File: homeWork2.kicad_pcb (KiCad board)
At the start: 2 copper layers, 36 parts, among them J4 0.100_2Pin, J5 0.100_2Pin, U1 LM7805_TO220

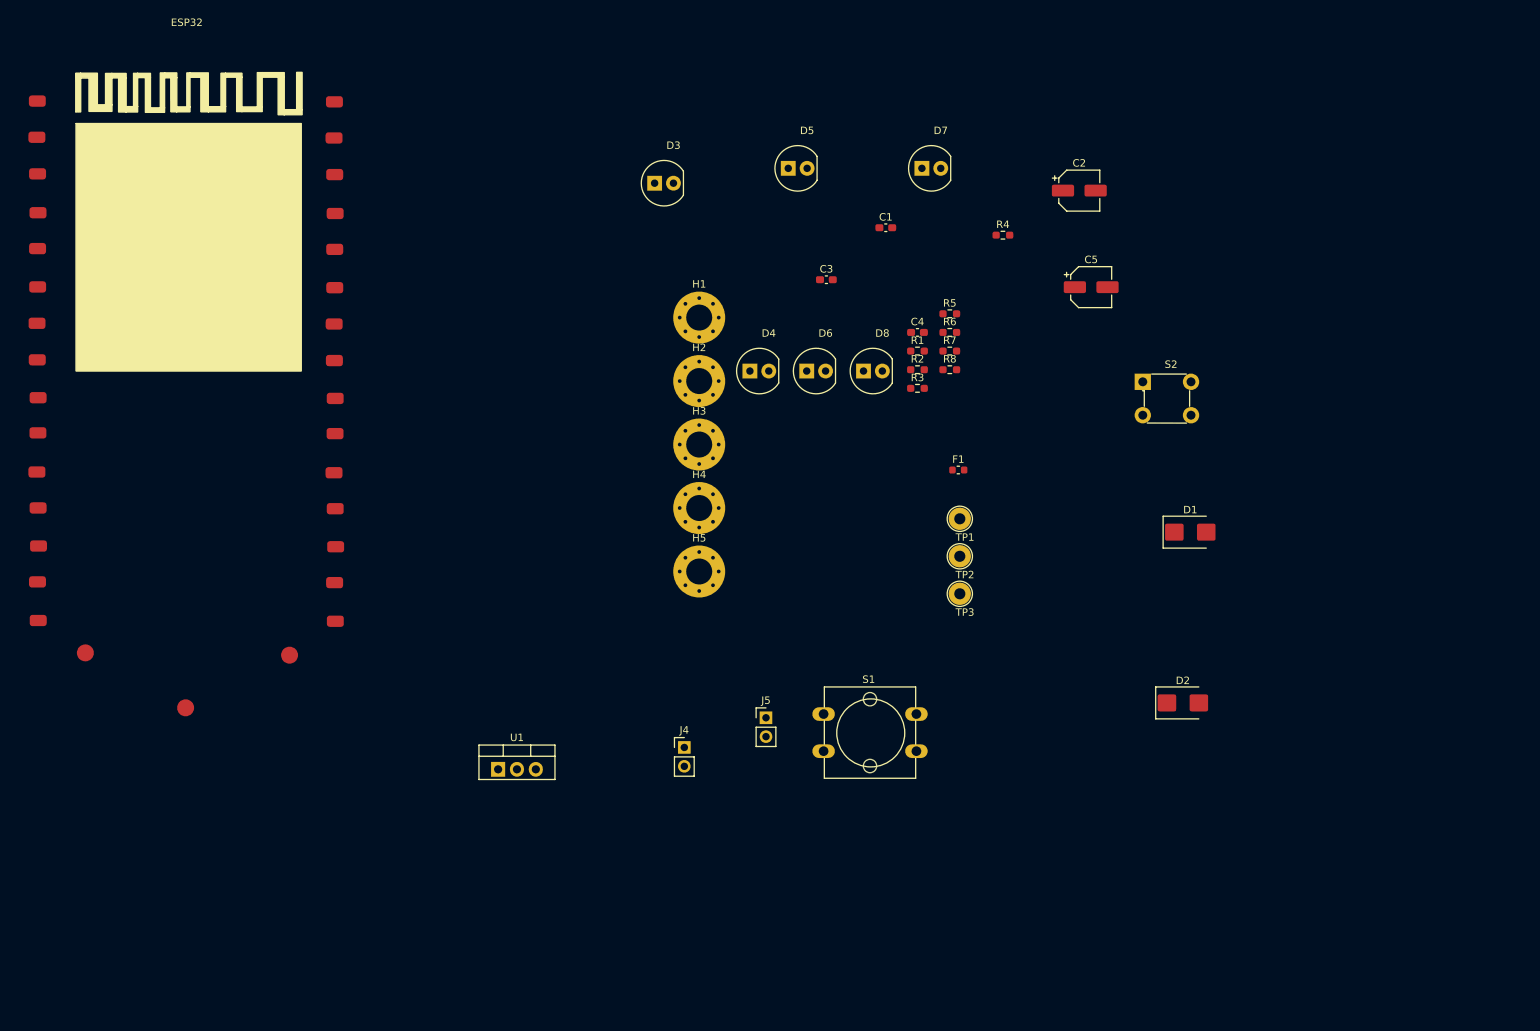
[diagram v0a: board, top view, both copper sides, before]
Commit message: Schematic changes
the ESP32 symbol library is not saved in the same folder of the project and linked to the footprint library
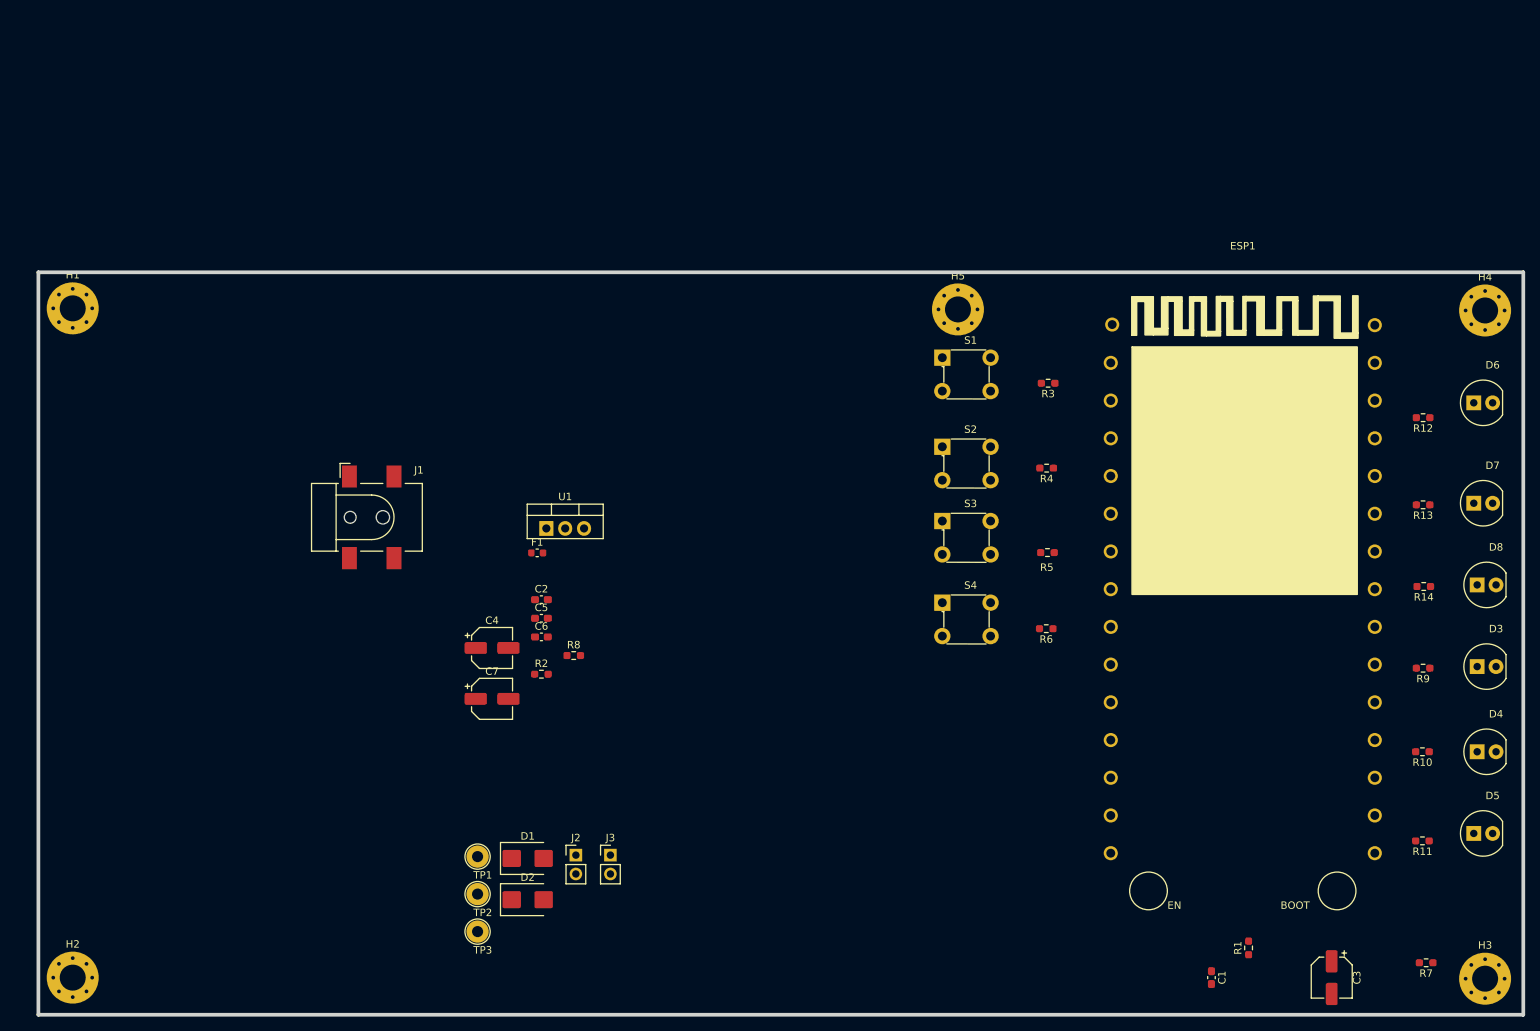
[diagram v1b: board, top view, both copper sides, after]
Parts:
- removed ESP32: ~, esp32 15 pin Library:esp32
- removed J4, J5: 0.100_2Pin, Connector_PinHeader_2.54mm:PinHeader_1x02_P2.54mm_Vertical
- added C6: 100nF, Capacitor_SMD:C_0603_1608Metric_Pad1.08x0.95mm_HandSolder, F.Cu at (117.8, 99.1)
- added C7: 47uF 16V, Capacitor_SMD:CP_Elec_5x5.4, F.Cu at (111.1, 107.5)
- added ESP1: ~, esp32 15 pin Library:esp32, F.Cu at (212.2, 47.0)
- added J1: Barrel_Jack_Switch_SMT, PubInv_KiCad_PCB:BarrelJack_CLIFF_FC681465S_SMT_Horizontal, F.Cu at (94.9, 83.0)
- added J2: 0.100_2Pin, Connector_PinHeader_2.54mm:PinHeader_1x02_P2.54mm_Vertical, F.Cu at (122.4, 128.5)
- added J3: 0.100_2Pin, Connector_PinHeader_2.54mm:PinHeader_1x02_P2.54mm_Vertical, F.Cu at (127.0, 128.5)
- added R10: 330R, Resistor_SMD:R_0603_1608Metric_Pad0.98x0.95mm_HandSolder, F.Cu at (236.4, 114.6)
- added R11: 330R, Resistor_SMD:R_0603_1608Metric_Pad0.98x0.95mm_HandSolder, F.Cu at (236.4, 126.6)
- added R12: 330R, Resistor_SMD:R_0603_1608Metric_Pad0.98x0.95mm_HandSolder, F.Cu at (236.5, 69.6)
- added R13: 330R, Resistor_SMD:R_0603_1608Metric_Pad0.98x0.95mm_HandSolder, F.Cu at (236.5, 81.3)
- added R14: 330R, Resistor_SMD:R_0603_1608Metric_Pad0.98x0.95mm_HandSolder, F.Cu at (236.6, 92.3)
- added R9: 330R, Resistor_SMD:R_0603_1608Metric_Pad0.98x0.95mm_HandSolder, F.Cu at (236.5, 103.3)
- added S3: SWITCH_TACTILE_SPST-NO_0.05A_24V, PubInv_KiCad_PCB:Switch_Tactile_THT_6x6mm, F.Cu at (171.8, 83.5)
- added S4: SWITCH_TACTILE_SPST-NO_0.05A_24V, PubInv_KiCad_PCB:Switch_Tactile_THT_6x6mm, F.Cu at (171.8, 94.5)
- C1: value 39pF -> 100nF
- C2: value 47uF 16V -> 39pF; footprint Capacitor_SMD:CP_Elec_5x5.4 -> Capacitor_SMD:C_0603_1608Metric_Pad1.08x0.95mm_HandSolder
- C3, C4: value 100nF -> 47uF 16V; footprint Capacitor_SMD:C_0603_1608Metric_Pad1.08x0.95mm_HandSolder -> Capacitor_SMD:CP_Elec_5x5.4
- C5: value 47uF 16V -> 100nF; footprint Capacitor_SMD:CP_Elec_5x5.4 -> Capacitor_SMD:C_0603_1608Metric_Pad1.08x0.95mm_HandSolder
- R1: value DNI -> 1R0
- R3, R4, R5, R6: value 330R -> 10K
- R7: value 330R -> 1R0
- R8: value 330R -> DNI
- S1: value SWITCH_TACTILE_12mmx12mm_SPST-NO_0.05A_24V -> SWITCH_TACTILE_SPST-NO_0.05A_24V; footprint PubInv_KiCad_PCB:SW_PUSH-12mm_WithCap_Green -> PubInv_KiCad_PCB:Switch_Tactile_THT_6x6mm
- moved D5 128.6 mm to (245.9, 125.6)
- moved D3 128.5 mm to (246.3, 103.1)
- moved H3 128.0 mm to (244.9, 145.1)
- moved H2 116.5 mm to (54.6, 145.0)
- moved C3 116.1 mm to (224.2, 145.0), turned to -90 degrees
- moved D4 110.6 mm to (246.3, 114.6)
- moved C1 110.1 mm to (208.0, 145.0), turned to -90 degrees
- moved H4 109.1 mm to (244.9, 55.1)
- moved R7 104.4 mm to (236.9, 143.0), turned to 180 degrees
- moved D1 99.5 mm to (115.9, 128.9)
- moved D2 92.1 mm to (115.9, 134.5)
- moved R1 91.9 mm to (213.0, 141.0), turned to 90 degrees
- moved C2 91.0 mm to (117.8, 94.1)
- moved D6 89.9 mm to (245.9, 67.6)
- moved D8 87.5 mm to (246.3, 92.1)
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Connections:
- C1 pad 1: GND -> Net-(ESP1-VIN)
- C2 pad 1: Vin -> GND
- C3 pad 1: Vin -> Net-(ESP1-VIN)
- C4 pad 1: +5V -> Vin
- C5 pad 1: +5V -> Vin
- F1 pad 2: GND -> Net-(F1-Pad2)
- R1 pad 1: ControllerVcc -> Net-(ESP1-VIN)
- R1 pad 2: Net-(D1-A) -> +5V
- R2 pad 1: VBus -> ControllerVcc
- R2 pad 2: +5V -> Net-(D1-A)
- R3 pad 1: Net-(D3-Pad1) -> Net-(ESP1-VP)
- R3 pad 2: Net-(ESP32-O15) -> +3.3V
- R4 pad 1: Net-(D4-Pad1) -> +3.3V
- R4 pad 2: Net-(ESP32-O15) -> Net-(ESP1-VN)
- R5 pad 1: Net-(D5-Pad1) -> +3.3V
- R5 pad 2: Net-(ESP32-O15) -> Net-(ESP1-O34)
- R6 pad 1: Net-(D6-Pad1) -> +3.3V
- R6 pad 2: Net-(ESP32-O18) -> Net-(ESP1-O35)
- R7 pad 1: Net-(D7-Pad1) -> Net-(ESP1-3V3)
- R7 pad 2: Net-(ESP32-O18) -> +3.3V
- R8 pad 1: Net-(D8-Pad1) -> VBus
- R8 pad 2: Net-(ESP32-O18) -> +5V
- S1 pad 1: Net-(ESP32-O15) -> GND
- S1 pad 2: Net-(ESP32-O15) -> GND
- S1 pad 3: GND -> Net-(ESP1-VP)
- S1 pad 4: GND -> Net-(ESP1-VP)
- S2 pad 1: Net-(ESP32-O18) -> GND
- S2 pad 2: Net-(ESP32-O18) -> GND
- S2 pad 3: GND -> Net-(ESP1-VN)
- S2 pad 4: GND -> Net-(ESP1-VN)
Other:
- board outline added: 200 x 100 mm

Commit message: PCB Update
Copper routing PCB components
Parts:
- added TP1: TP_GND, TestPoint:TestPoint_Loop_D2.54mm_Drill1.5mm_Beaded, F.Cu at (159.0, 73.0)
- moved R7 112.0 mm to (133.1, 101.0)
- moved J1 81.5 mm to (169.9, 115.0)
- moved H2 75.8 mm to (130.4, 142.0)
- moved H1 75.8 mm to (130.4, 55.0)
- moved TP1 65.0 mm to (159.0, 87.0)
- moved C2 64.6 mm to (162.0, 141.1), turned to 90 degrees
- moved C4 59.2 mm to (163.0, 129.0)
- moved C6 56.7 mm to (156.0, 141.0), turned to -90 degrees
- moved R8 51.8 mm to (160.0, 136.9)
- moved F1 47.5 mm to (158.0, 112.0), turned to 90 degrees
- moved C7 43.1 mm to (144.2, 135.0), turned to 180 degrees
- moved D2 40.8 mm to (154.0, 120.0), turned to 90 degrees
- moved C3 40.4 mm to (186.0, 132.0), turned to 180 degrees
- moved TP3 39.6 mm to (134.0, 108.0)
- moved C5 38.6 mm to (145.0, 124.0)
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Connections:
- ESP1 pad 14: GND -> unconnected-(ESP1-GND-Pad14)
- ESP1 pad 17: unconnected-(ESP1-GND-Pad17) -> GND
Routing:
- net GND: track 0.00 -> 625.6 mm
- net +3.3V: track 0.00 -> 227.9 mm
- net Net-(ESP1-3V3): track 0.00 -> 209.6 mm
- net +5V: track 0.00 -> 140.9 mm
- net Vin: track 0.00 -> 49.9 mm
- net Net-(ESP1-O35): track 0.00 -> 44.6 mm
- net Net-(ESP1-O34): track 0.00 -> 36.0 mm
- net Net-(ESP1-VP): track 0.00 -> 31.6 mm
- net Net-(ESP1-VN): track 0.00 -> 29.2 mm
- net Net-(ESP1-VIN): track 0.00 -> 18.2 mm
- net Net-(D1-A): track 0.00 -> 15.9 mm
- net Net-(F1-Pad2): track 0.00 -> 15.6 mm
- net Net-(ESP1-O19): track 0.00 -> 15.6 mm
- net Net-(ESP1-O15): track 0.00 -> 12.6 mm
- net ControllerVcc: track 0.00 -> 11.7 mm
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- added copper zone on F.Cu, net (none)
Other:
- board size 200 x 100 mm -> 130 x 100 mm

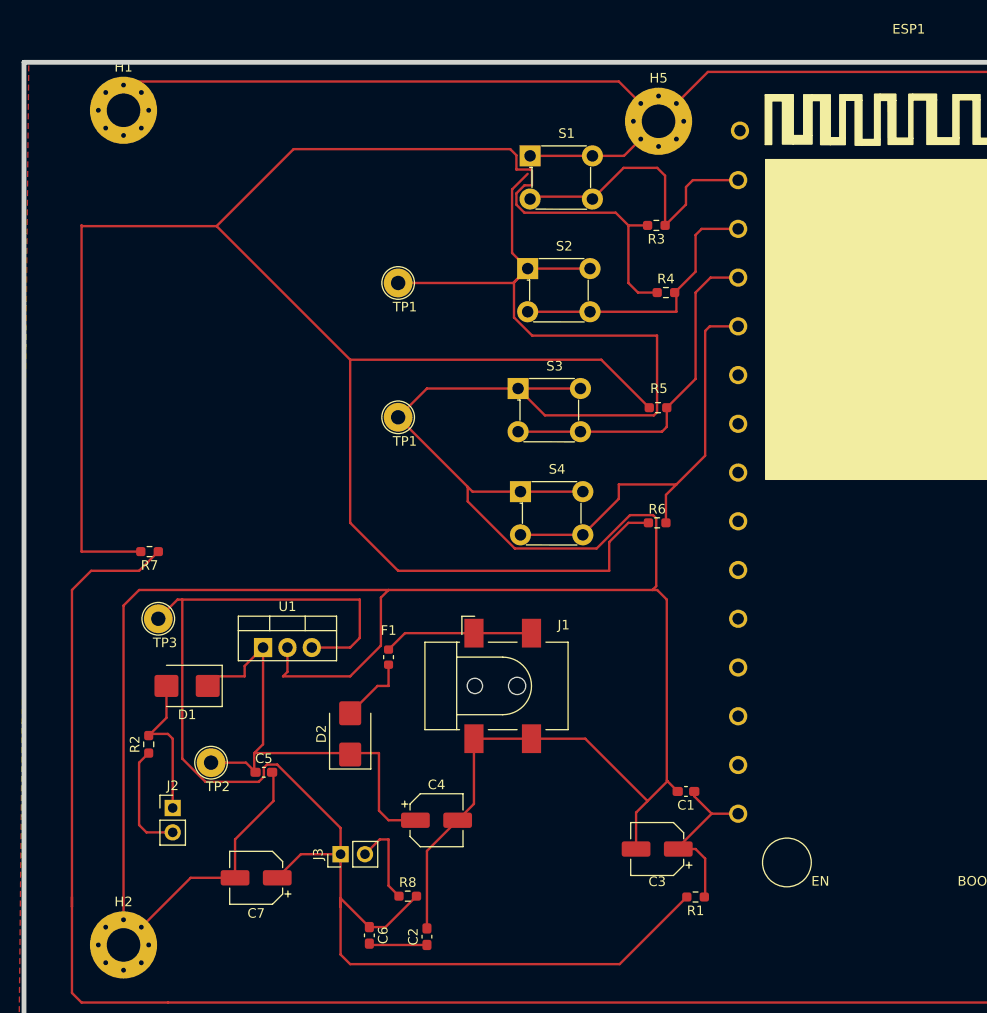
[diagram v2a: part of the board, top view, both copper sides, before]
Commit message: this is to clean the deleted backup files and to update the modified pcb file where I attached the copper fill to ground and added text to the silkscreen and to update the sch files where I added the date and the serial number space in the origin main branch.
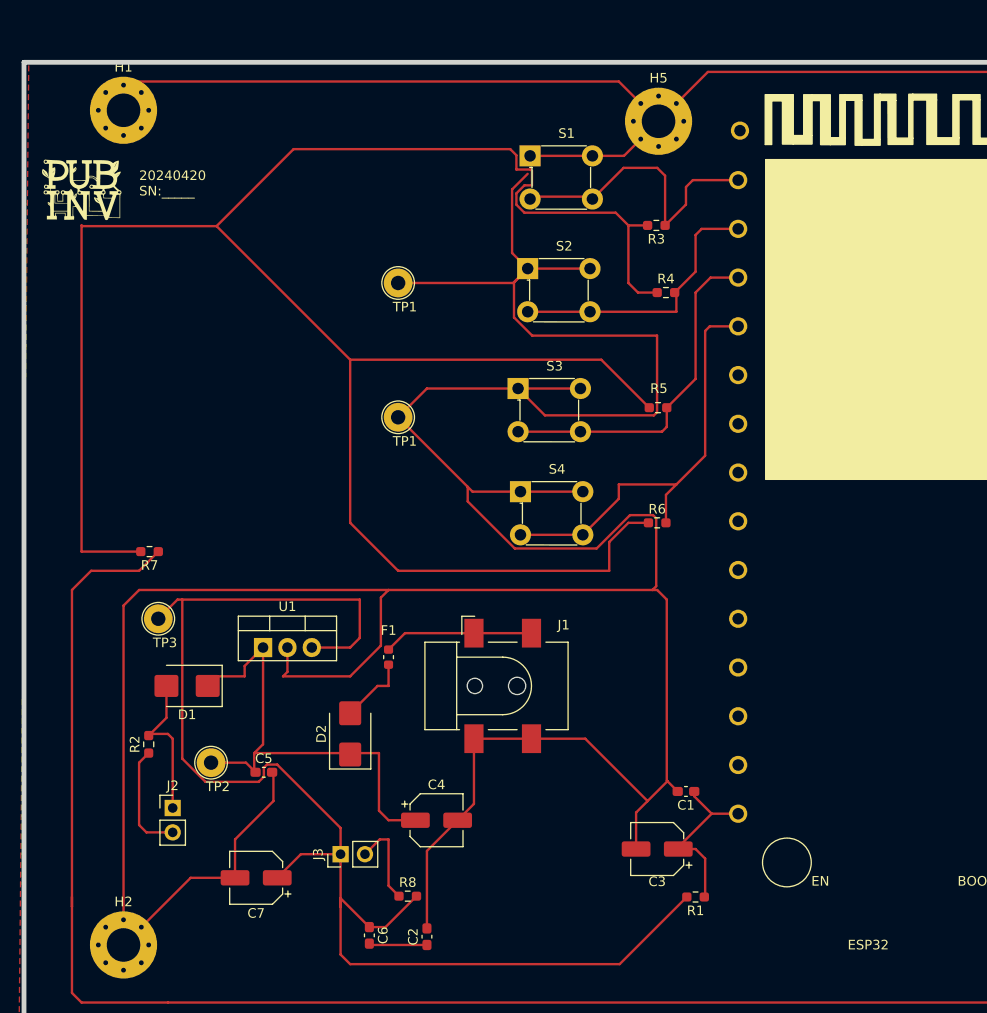
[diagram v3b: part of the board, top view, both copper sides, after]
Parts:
- added G***: LOGO, PubInv_KiCad_PCB:Logo_PI_BandW_70percent_10x10, F.Cu at (126.0, 63.5)
- ESP32: renamed from ESP1; value ~ -> Wroom ESP32
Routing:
- added copper zone on F.Cu, net GND
- removed copper zone on F.Cu, net (none)
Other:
- board text added: "20240420 SN:_____"
